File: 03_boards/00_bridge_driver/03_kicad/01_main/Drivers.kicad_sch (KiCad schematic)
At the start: 33 parts, among them Q1 SUD90330E, Q2 SUD90330E, Q3 SUD90330E, Q4 SUD90330E, Q5 SUD90330E, Q6 SUD90330E, U1 IR2104, U2 IR2104, U3 IR2104

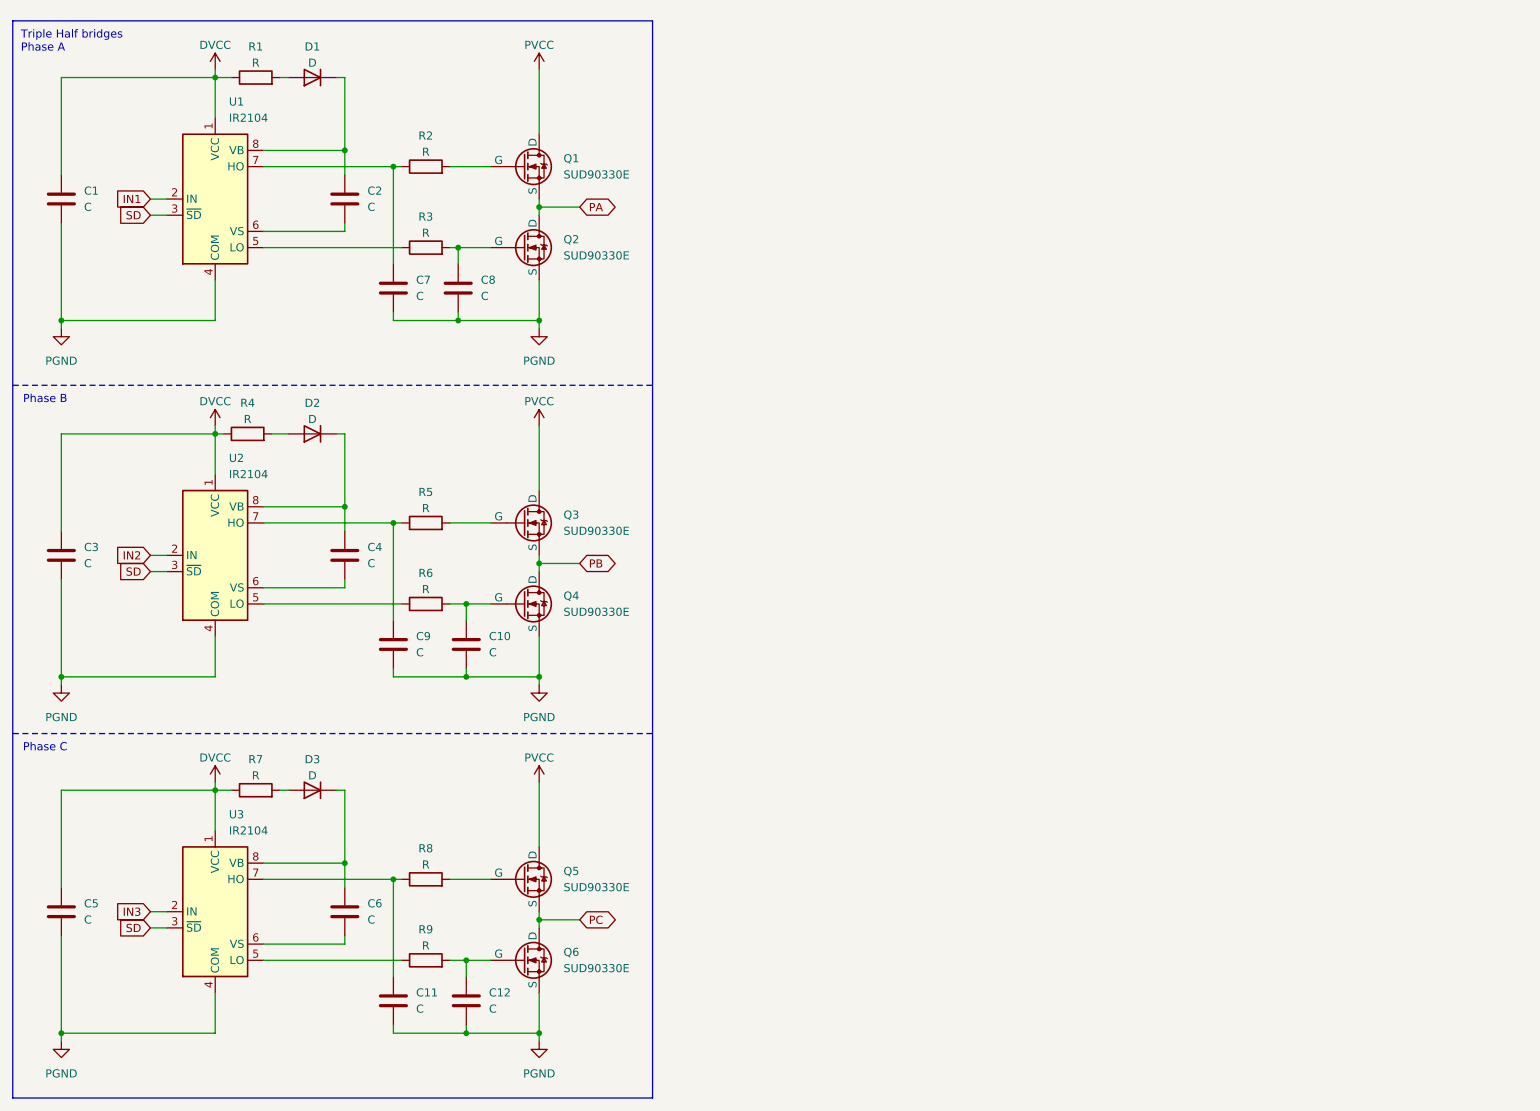
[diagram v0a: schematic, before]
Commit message: Week 0x4 - Spatial ROMs are hard.... (#25)
* Reference document with bootstrap selection calculations

* Boot strap capacitors, resistors and diode work for triple half bridge driver

* Few small changes to reduced order model

* Reduced order model under FOC control

* Finished initial reduced order model

* Custom motor model that needs to be validated and graphs

* Rename to 00_reduced_order_model and Updated readme.md

* Few changes to the model model & Selected Boot Diodes

* Began work on the refactored reduced order model

* New parameter file, removed library and added derived equations

* Initial draft of reduced order model

* Moving pole equation around. Solver not working.

* Issues with the field modelling

* Few additional changes before merge
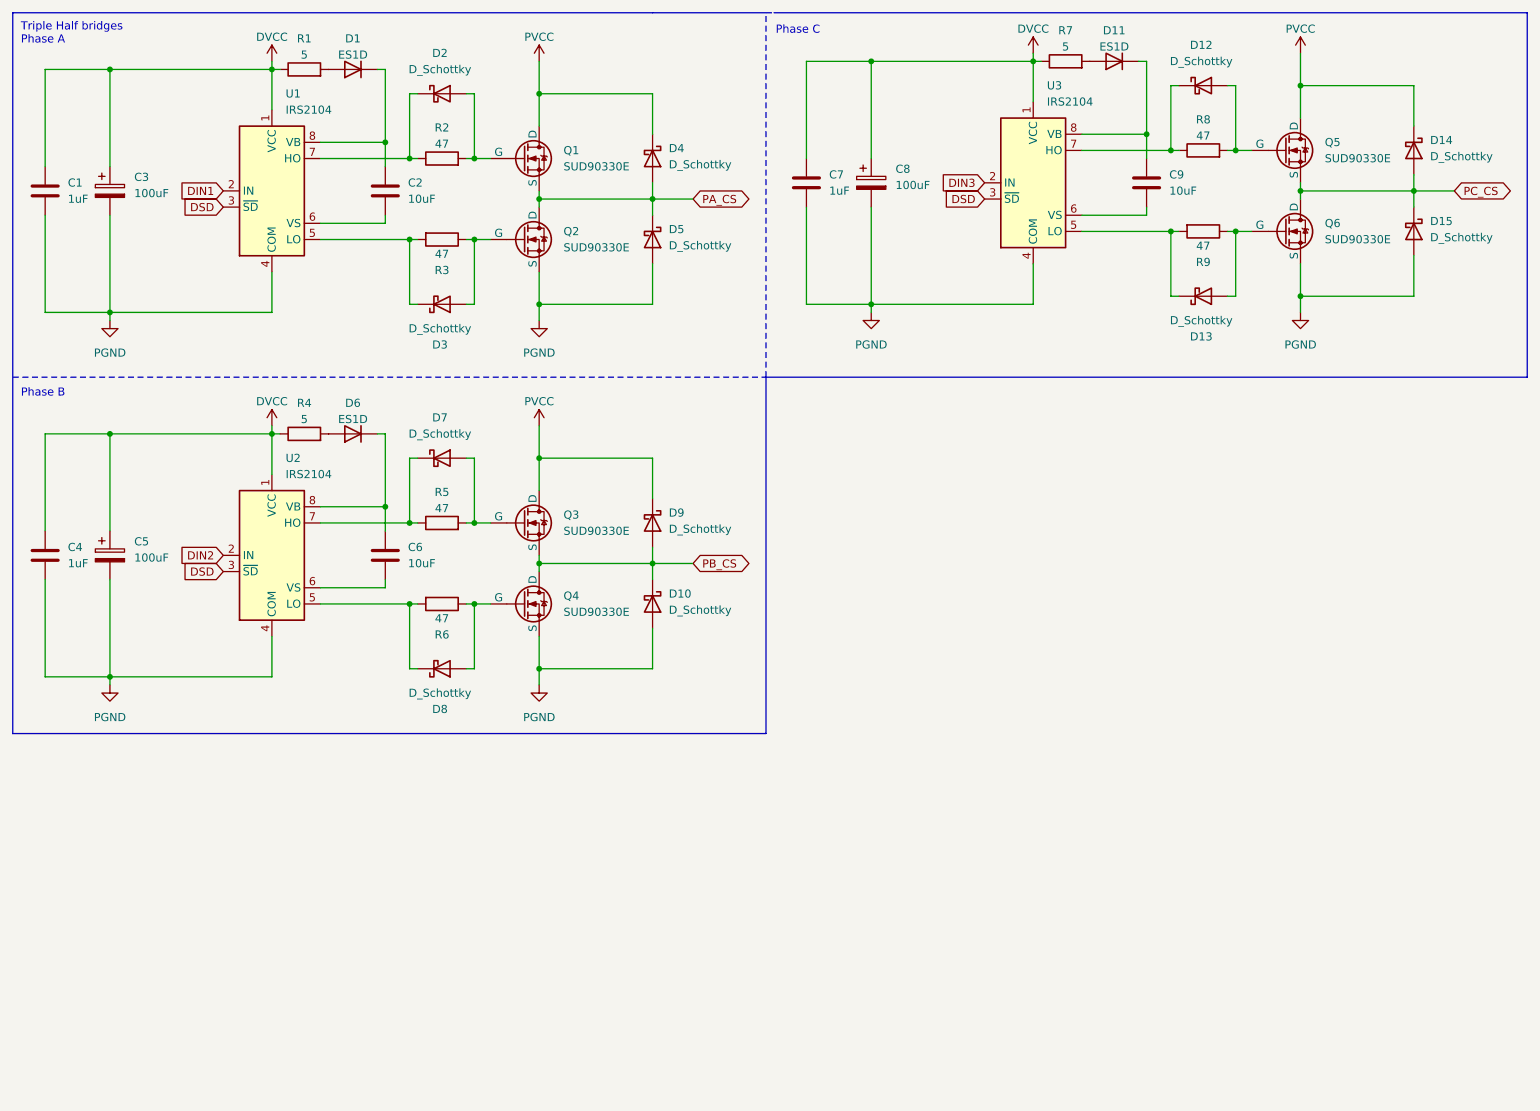
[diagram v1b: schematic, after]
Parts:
- removed C10, C11, C12, C3, C5, C8: C, symbol Device:C
- removed D2, D3: D, symbol Device:D
- added C3, C5, C8: 100uF, symbol Device:C_Polarized
- added D10, D12, D13, D14, D15, D2, D3, D4, D5, D7, D8, D9: D_Schottky, symbol Device:D_Schottky
- added D11, D6: ES1D, symbol Device:D
- C1, C4, C7: value C -> 1uF
- C2, C6, C9: value C -> 10uF
- D1: value D -> ES1D
- R1, R4, R7: value R -> 5
- R2, R3, R5, R6, R8, R9: value R -> 47
- U1, U2, U3: value IR2104 -> IRS2104
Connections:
- net DVCC: now also C4.1, C7.1, C3.1, C5.1, C8.1
- net PGND: now also C4.2, C3.2, C5.2, C8.2, D10.2 (A), D15.2 (A), D5.2 (A); no longer C9.2
- net PVCC: now also D14.1 (K), D4.1 (K), D9.1 (K)
- net at R9.2: now also U3.5 (LO), D13.1 (K); no longer Q6.2 (G)
- net at R8.1, U3.7 (HO): now also D12.1 (K)
- net at U2.5 (LO): now also R6.2, D8.1 (K); no longer R6.1
- net at U2.6 (VS): now also C6.2; no longer C4.2
- net at R5.1, U2.7 (HO): now also D7.1 (K); no longer C9.1
- net at U2.8 (VB): now also C6.1, D6.1 (K); no longer C4.1
- net at R3.2: now also U1.5 (LO), D3.1 (K); no longer Q2.2 (G)
- net at Q5.2 (G), R8.2: now also D12.2 (A)
- net at R2.1, U1.7 (HO): now also D2.1 (K); no longer C7.1
- net at Q1.2 (G), R2.2: now also D2.2 (A)
- net at R9.1: now also Q6.2 (G), D13.2 (A); no longer U3.5 (LO)
- net at U3.6 (VS): now also C9.2; no longer C6.2
- net at U3.8 (VB): now also C9.1, D11.1 (K); no longer C6.1
- net at Q4.2 (G): now also R6.1, D8.2 (A); no longer R6.2
- net at R7.2: now also D11.2 (A)
- net at R4.2: now also D6.2 (A)
- net at Q3.2 (G), R5.2: now also D7.2 (A)
- net at R3.1: now also Q2.2 (G), D3.2 (A); no longer U1.5 (LO)
- net IN1 renamed DIN1
- net IN2 renamed DIN2
- net IN3 renamed DIN3
- net PA renamed PA_CS
- net PA_CS: now also D4.2 (A), D5.1 (K)
- net PB renamed PB_CS
- net PB_CS: now also D10.1 (K), D9.2 (A)
- net PC renamed PC_CS
- net PC_CS: now also D14.2 (A), D15.1 (K)
- net SD renamed DSD
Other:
- title: Triple half bridge drivers and switches -> (none)

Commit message: Week 0x7 | Streamlining deliverables (#31)
* Updated links and added note to BOM

* Fixed links

* Triple bridge driver layout

* Updated the readmes a bit and moved the analytical to 00_analytical

* Added notes about revision 3

* Added note about quality of the images

* Noted that prototype beta revision 2 is specifically not for fabrication.

* Added a note about revision 3

* Added break line

* Moved contributors and credits to /04_docs and also updated > sections

* Restructured the simulation section and simplified deliverables

* Improved documentation section at the bottom of the readme and improved 04_docs

* Updated readme.md

* Removed note.

* Fixed error with boards readme.md

* Added note about images requiring updates

* Add images to the readmes of a few sections

* Fixed point for new objective entry
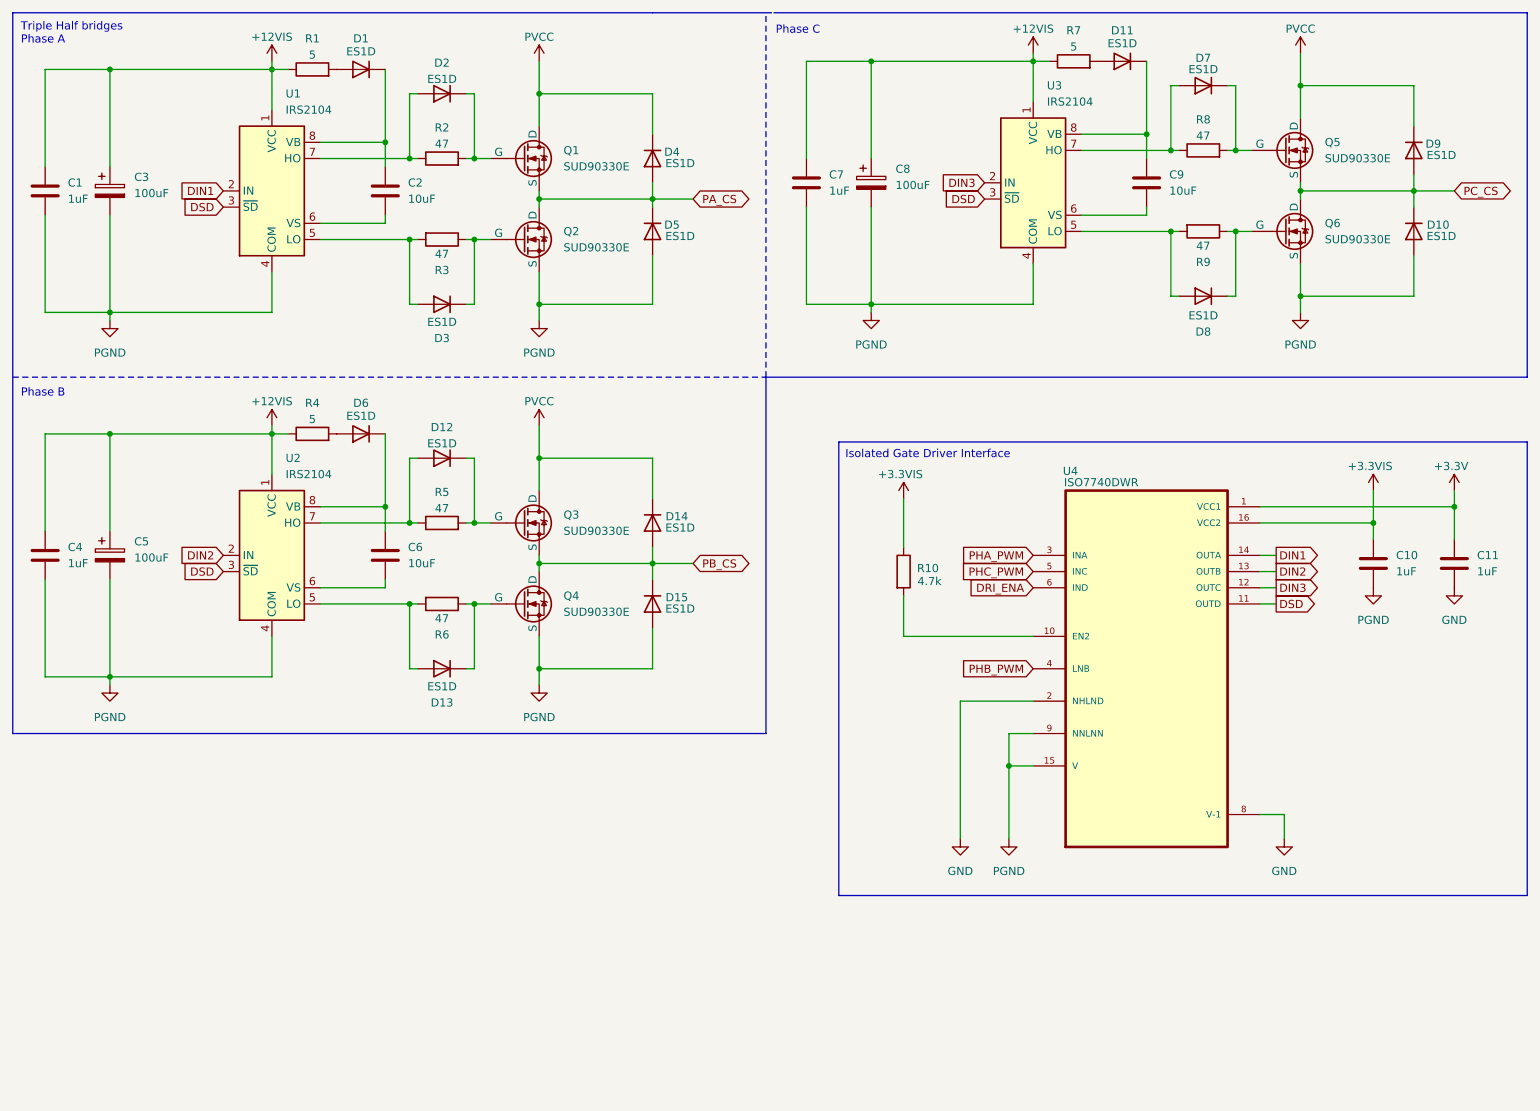
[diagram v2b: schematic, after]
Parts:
- removed D10, D12, D13, D14, D15, D2, D3, D4, D5, D7, D8, D9: D_Schottky, symbol Device:D_Schottky
- added C10, C11: 1uF, symbol Device:C
- added D10, D12, D13, D14, D15, D2, D3, D4, D5, D7, D8, D9: ES1D, symbol Device:D
- added R10: 4.7k, symbol Device:R
- added U4: ISO7740DWR, ISO7740DWR:SOIC127P1030X265-16N, symbol 2026-07-25_11-21-53:ISO7740DWR
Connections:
- net DIN1: now also U4.14 (OUTA)
- net DIN2: now also U4.13 (OUTB)
- net DIN3: now also U4.12 (OUTC)
- net DSD: now also U4.11 (OUTD)
- net PA_CS: now also D4.2 (A), D5.1 (K)
- net PB_CS: now also D14.2 (A), D15.1 (K)
- net PC_CS: now also D10.1 (K), D9.2 (A)
- net PGND: now also C10.2, D10.2 (A), D15.2 (A), D5.2 (A), U4.15 (V), U4.9 (NNLNN)
- net PVCC: now also D14.1 (K), D4.1 (K), D9.1 (K)
- net at Q5.2 (G), R8.2: now also D7.1 (K)
- net at R3.2, U1.5 (LO): now also D3.2 (A)
- net at R2.1, U1.7 (HO): now also D2.2 (A)
- net at Q1.2 (G), R2.2: now also D2.1 (K)
- net at R8.1, U3.7 (HO): now also D7.2 (A)
- net at R5.1, U2.7 (HO): now also D12.2 (A)
- net at Q3.2 (G), R5.2: now also D12.1 (K)
- net at R6.2, U2.5 (LO): now also D13.2 (A)
- net at Q4.2 (G), R6.1: now also D13.1 (K)
- net at Q2.2 (G), R3.1: now also D3.1 (K)
- net at R9.2, U3.5 (LO): now also D8.2 (A)
- net at Q6.2 (G), R9.1: now also D8.1 (K)
- net DVCC renamed +12VIS
- new net: R10.2, U4.10 (EN2)
- new net +3.3V: C11.1, U4.1 (VCC1)
- new net +3.3VIS: C10.1, R10.1, U4.16 (VCC2)
- new net DRI_ENA: U4.6 (IND)
- new net GND: C11.2, U4.2 (NHLND), U4.8 (V-1)
- new net PHA_PWM: U4.3 (INA)
- new net PHB_PWM: U4.4 (LNB)
- new net PHC_PWM: U4.5 (INC)
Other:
- note added: "Isolated Gate Driver Interface"
- title: (none) -> Phase Drivers & Isolation
- moved on the sheet: D1, D11, D6, R1, R4, R7

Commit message: Alot of the schematic finished
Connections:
- net at Q5.2 (G), R8.2: now also D7.2 (A); no longer D7.1 (K)
- net at R3.2, U1.5 (LO): now also D3.1 (K); no longer D3.2 (A)
- net at R2.1, U1.7 (HO): now also D2.1 (K); no longer D2.2 (A)
- net at Q1.2 (G), R2.2: now also D2.2 (A); no longer D2.1 (K)
- net at R5.1, U2.7 (HO): now also D12.1 (K); no longer D12.2 (A)
- net at Q3.2 (G), R5.2: now also D12.2 (A); no longer D12.1 (K)
- net at Q6.2 (G), R9.1: now also D8.2 (A); no longer D8.1 (K)
- net at R9.2, U3.5 (LO): now also D8.1 (K); no longer D8.2 (A)
- net at R6.2, U2.5 (LO): now also D13.1 (K); no longer D13.2 (A)
- net at Q2.2 (G), R3.1: now also D3.2 (A); no longer D3.1 (K)
- net at R8.1, U3.7 (HO): now also D7.1 (K); no longer D7.2 (A)
- net at Q4.2 (G), R6.1: now also D13.2 (A); no longer D13.1 (K)
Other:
- moved on the sheet: C10, C11, D12, D2, D7, R10, U4

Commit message: Simulation for current sensors and such
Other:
- note added: "F, C"
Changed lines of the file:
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@@
 	(title_block
 		(title "Phase Drivers & Isolation")
+		(rev "0")
 	)
 	(text "Isolated Gate Driver Interface\n"
@@
 			)
 			(justify left)
+		)
+	)
+	(text "F, C"
+		(exclude_from_sim no)
+		(at 145.034 68.834 0)
+		(effects
+			(font
+				(size 1.27 1.27)
+			)
+		)
+	)
+	(text "F, C"
+		(exclude_from_sim no)
+		(at 51.308 91.186 0)
+		(effects
+			(font
+				(size 1.27 1.27)
+			)
 		)
 	)
@@
 		)
 	)
+	(text "F, C"
+		(exclude_from_sim no)
+		(at 148.59 91.44 0)
+		(effects
+			(font
+				(size 1.27 1.27)
+			)
+		)
+	)
+	(text "F, C"
+		(exclude_from_sim no)
+		(at 72.898 70.612 0)
+		(effects
+			(font
+				(size 1.27 1.27)
+			)
+		)
+	)
